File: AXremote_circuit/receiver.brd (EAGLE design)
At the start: 90 x 59 mm, 68 parts, among them IC1 MEGA8-AI, Q1 16MHz, Q2 12MHz, Q3 MOSFET-NCHANNELBSS138, U1 AX8052F143HS, X1 MINI-USB-SCHIELD-32005-201

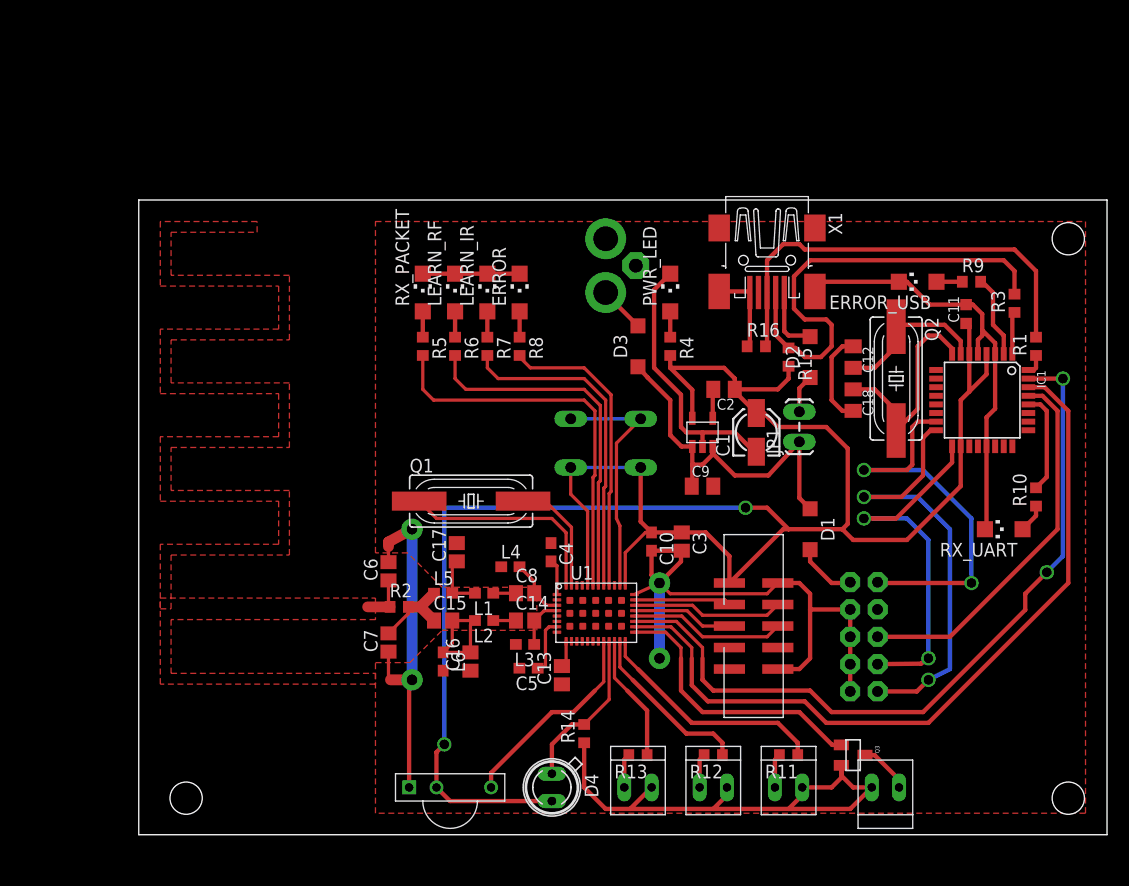
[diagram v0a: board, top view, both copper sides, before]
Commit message: Added a few keys.
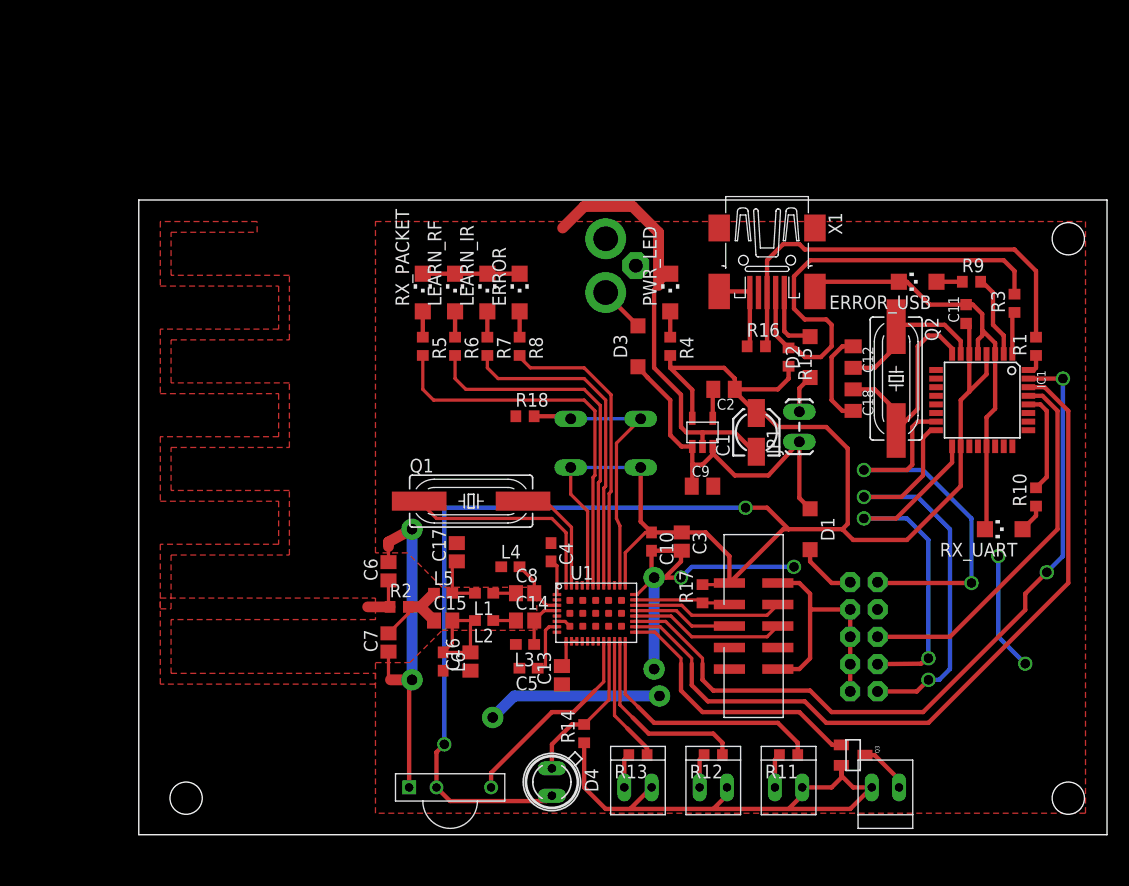
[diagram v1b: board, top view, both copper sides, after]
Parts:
- added R17, R18: 100, resistor:R0603
- moved D4 0.50 mm to (39.0, 5.50)
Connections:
- net GND: now also R18.1
- net N$27: now also R18.2
- net RST_N: now also R17.1
- net VCC: now also R17.2
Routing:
- net GND: track 234.6 -> 280.6 mm, vias 4 -> 10
- net N$27: track 23.0 -> 26.5 mm
- net VCC: track 199.0 -> 201.7 mm
- net N$40: track 16.0 -> 18.0 mm
- net N$39: track 21.9 -> 24.0 mm
- net N$47: track 25.9 -> 25.3 mm
- net UART_AXOUT: track 72.1 -> 71.5 mm
- net UART_AXIN: track 71.7 -> 71.1 mm
- net N$46: track 15.2 -> 14.7 mm
- net N$1: track 0.00 -> 0.50 mm

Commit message: Start work on receiver rev2.
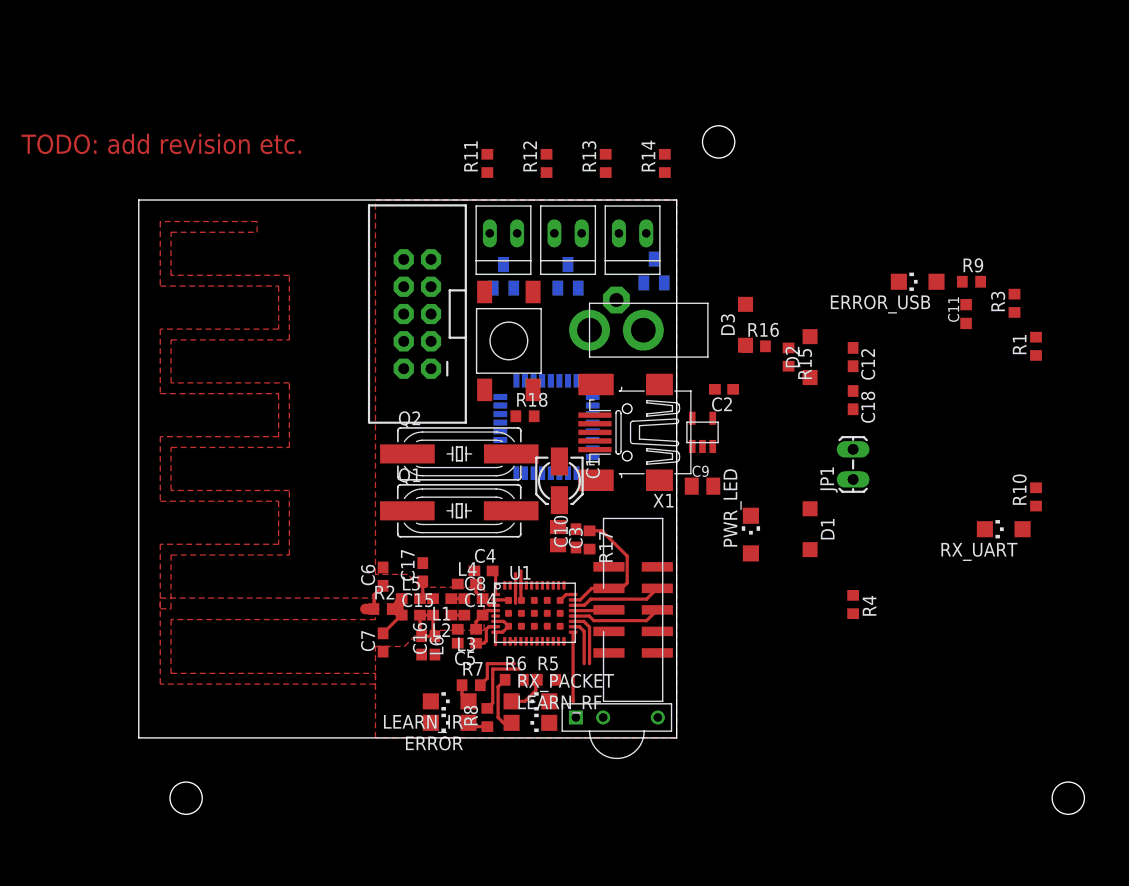
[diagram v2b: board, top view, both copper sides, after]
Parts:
- removed C13: 39pF, resistor:C0805
- removed D4: SFH482, led:SFH482
- removed S1: (no value), switch-omron:B3F-10XX
- added Q4, Q5: BC849SMD, transistor-npn:SOT23-BEC
- C12, C18, C2: device resistor:C0805K -> resistor:C0603
- C14, C15, C16, C17, C6, C7, C8: device resistor:C0805 -> resistor:C0603
- R12: value 100 -> ?
- R17: value 100 -> 10k
- U$7: value IR LED -> SWITCHSMD; device sam_eagle_parts:2PIN_PINHEADER -> sam:TACTILE_SWITCH_FSM2JSMA
- moved U$9 62.5 mm to (34.5, 56.5)
- moved R11 61.7 mm to (33.0, 63.0), turned to 90 degrees
- moved R12 57.1 mm to (38.5, 63.0), turned to 90 degrees
- moved Q3 55.1 mm to (34.5, 52.5), flipped to the bottom, turned to 0 degrees
- moved R13 55.1 mm to (44.0, 63.0), turned to 90 degrees
- moved R14 53.5 mm to (49.5, 63.0)
- moved U$5 53.5 mm to (46.5, 56.5), turned to 180 degrees
- moved U$6 53.2 mm to (40.5, 56.5), turned to 180 degrees
- moved U$2 51.2 mm to (26.5, 49.0), flipped to the top, turned to 180 degrees
- moved U$7 43.2 mm to (35.0, 46.5)
- moved Q2 41.2 mm to (30.4, 36.0), turned to 0 degrees
- moved LEARN_RF 40.6 mm to (37.0, 11.0), turned to 270 degrees
- moved IC1 40.6 mm to (38.5, 38.5), flipped to the bottom
- moved ERROR 40.5 mm to (29.5, 11.0), turned to 90 degrees
- moved RX_PACKET 39.3 mm to (37.0, 13.0), turned to 270 degrees
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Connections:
- removed net N$2: C13.2, U1.9
- removed net N$46: D4.A, R14.2, U1.17
- net GND: now also Q4.E, Q5.E, R14.2; no longer C13.1, R14.1, U$5.P$2, U$6.P$2, U$7.P$2
- net N$27: now also U$7.P3, U$7.P4; no longer S1.3, S1.4
- net N$39: now also Q4.C, U$5.P$2; no longer R11.1, U1.20
- net N$40: now also R13.1, U$6.P$1; no longer R12.1, U1.19
- net N$41: now also Q5.C, U$6.P$2; no longer R13.1, U1.18
- net N$42: now also R12.1, U1.20; no longer R13.2, U$7.P$1
- net N$43: now also Q4.B, Q5.B, R14.1; no longer U$6.P$1
- net VCC: now also R11.1, R13.2, U$7.P1, U$7.P2; no longer D4.K, S1.1, S1.2
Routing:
- net GND: track 280.6 -> 15.4 mm, vias 10 -> 0
- net VCC: track 201.7 -> 0.00 mm, vias 2 -> 0
- net UART_AXOUT: track 71.5 -> 4.21 mm
- net UART_AXIN: track 71.1 -> 5.15 mm, vias 2 -> 0
- net D-: track 43.2 -> 0.00 mm
- net N$21: track 41.2 -> 0.00 mm, vias 2 -> 0
- net D+: track 40.9 -> 0.00 mm
- net N$23: track 37.2 -> 0.00 mm, vias 2 -> 0
- net N$26: track 36.3 -> 0.00 mm
- net N$19: track 35.2 -> 0.00 mm
- net N$22: track 34.6 -> 0.00 mm, vias 2 -> 0
- net VCC_IN: track 34.4 -> 0.00 mm
- net N$31: track 33.5 -> 0.00 mm
- net N$27: track 26.5 -> 0.00 mm
- net N$32: track 30.7 -> 4.77 mm
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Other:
- board size 90 x 59 mm -> 50 x 50 mm
- board text added: "TODO: add revision etc."

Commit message: Replace AVR with FT121 on receiver. Other details.
- Clean up schematics
- Use every pin of F143 (second button, GPIO)
- add TXCO and XTAL
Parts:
- removed D1, D2, D3: (no value), diode:SOD123
- removed ERROR_USB: rot, led:CHIPLED_1206
- removed IC1: MEGA8-AI, atmel:TQFP32-08
- removed Q2: 12MHz, crystal:SM49
- removed Q4: BC849SMD, transistor-npn:SOT23-BEC
- removed RX_UART: grün, led:CHIPLED_1206
- added BEAD: ferrite, resistor:R0603
- added C13: 47pF, resistor:C0603K
- added C19: 100nF, resistor:C0603K
- added C20, C21: 100n, resistor:C0603
- added R19: 10k, resistor:R0603
- added U$10: SWITCHSMD, sam:TACTILE_SWITCH_FSM2JSMA
- added X2: (no value), axsem_osc_v1-2:X3225
- C12: value 27pF -> 47pF; device resistor:C0603 -> resistor:C0603K
- C18: value 27pF -> 10nF; device resistor:C0603 -> resistor:C0603K
- JP1: value M02LOCK_LONGPADS -> (none); device SparkFun-Connectors:1X02_LOCK_LONGPADS -> jumper:JP2
- R1, R3: value 68 -> 27
- R10: value 68 -> 10k
- R15: value 1k5 -> 100
- R16: value 1M -> NC
- R9: value 100 -> 10k
- U$2: value AVR_SPI_PROG2PTH2 -> FT121; device SparkFun-Connectors:2X5-SHROUDED -> sam:TSSOP16
- moved R10 59.5 mm to (26.2, 46.2), turned to 0 degrees
- moved R15 57.6 mm to (25.0, 0.00), turned to 0 degrees
- moved R9 51.8 mm to (26.2, 51.4)
- moved C12 47.2 mm to (26.2, 68.8), turned to 0 degrees
- moved C18 45.2 mm to (26.2, 60.4), turned to 0 degrees
- moved JP1 42.7 mm to (34.5, 6.00), turned to 180 degrees
- moved R16 29.3 mm to (31.5, 33.5)
- moved U$1 18.9 mm to (38.0, 49.5)
- moved U$2 15.2 mm to (36.5, 37.5), turned to 90 degrees
- moved C1 13.4 mm to (27.0, 37.7), turned to 0 degrees
- moved R18 9.55 mm to (27.0, 40.5)
- moved U$7 2.06 mm to (33.0, 47.0)
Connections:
- removed net N$23: IC1.15, U$2.1
- removed net N$24: D1.A, U$2.2
- removed net N$34: ERROR_USB.A, R9.1
- removed net N$35: IC1.2, R9.2
- removed net N$36: R10.1, RX_UART.A
- removed net N$38: D3.A, U$4.P1:PIN
- removed net N$39: Q4.C, U$5.P$2
- removed net N$45: U$8.P3:OUT, U1.16
- removed net N$49: D2.C, JP1.2
- removed net N$50: IC1.28, R10.2
- removed net UART_AXIN: IC1.31, U1.23
- removed net UART_AXOUT: IC1.30, U1.22
- new net FTDI_!RESET: R9.2, U$2.11, U1.18
- new net FTDI_SUSPEND: R10.2, U$2.6, U1.19
- new net N$2: R1.1, U$2.16
- new net SPI_!INT: U$2.7, U1.13
- new net SPI_!SS: U$2.3, U1.17
- new net SPI_MISO: U$2.8, U1.14
- new net SPI_MOSI: U$2.9, U1.15
- new net SPI_SCLK: U$2.2, U1.16
- net D+: now also C13.1; no longer R16.2
- net D-: now also C12.1; no longer R15.1
- net GND: now also C12.2, C13.2, C18.1, C19.1, C20.2, JP1.3, R15.1, U$2.14, X2.2; no longer C12.1, C18.2, ERROR_USB.C, IC1.21, IC1.3, IC1.5, Q4.E, RX_UART.C, U$2.10, U$2.6, U$2.8
- net N$11: now also BEAD.1, C11.1, U$2.13; no longer C18.1, IC1.8, Q2.2
- net N$14: now also R19.2
- net N$15: now also C21.1, R19.1
- net N$16: now also JP1.1, U1.22; no longer IC1.32, R1.1
- net N$17: now also R15.2, U$10.P3, U$10.P4, U1.31; no longer IC1.1, R3.1
- net N$19: now also R16.2, X2.1; no longer IC1.29, U$2.5
- net N$21: now also U$8.P3:OUT, U1.21; no longer IC1.16, U$2.9
- net N$22: now also C21.2, X2.3; no longer IC1.17, U$2.7
- net N$41: now also U$5.P$2
- net N$43: no longer Q4.B
- net N$47: now also U1.23; no longer U1.21
- net N$5: now also R3.1, U$2.15; no longer C12.2, IC1.7, Q2.1
- net VCC: now also C19.2, C20.1, JP1.2, R10.1, R9.1, U$10.P1, U$10.P2, U$2.10, U$2.12, U$2.5, X2.4; no longer C11.1, IC1.18, IC1.4, IC1.6, R15.2
- net VCC_IN: now also U$4.P1:PIN; no longer D1.C, D3.C, JP1.1
- net VCC_USB: now also BEAD.2, C18.2; no longer D2.A
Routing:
- net N$47: track 6.44 -> 0.00 mm
- net UART_AXIN: track 5.15 -> 0.00 mm
- net UART_AXOUT: track 4.21 -> 0.00 mm
- net RST_N: track 12.7 -> 10.8 mm
- net DBG_DATA: track 8.42 -> 7.01 mm

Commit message: Started routing receiver rev2.
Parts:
- U$2: value FT121 -> FT121FTDI; device sam:TSSOP16 -> sam:TSSOP16-FTDI
- moved R15 48.1 mm to (32.5, 47.5), turned to 90 degrees
- moved R1 44.8 mm to (39.8, 38.4), turned to 0 degrees
- moved R3 44.2 mm to (39.8, 37.0), turned to 0 degrees
- moved C11 42.5 mm to (37.2, 35.4), turned to 270 degrees
- moved ERROR 41.3 mm to (64.5, 33.0), turned to 180 degrees
- moved LEARN_RF 40.3 mm to (64.5, 40.5), turned to 0 degrees
- moved BEAD 40.2 mm to (39.8, 35.6)
- moved R8 39.8 mm to (64.0, 36.5), turned to 180 degrees
- moved R9 39.2 mm to (38.0, 14.0)
- moved LEARN_IR 38.6 mm to (62.5, 33.0), turned to 180 degrees
- moved RX_PACKET 37.5 mm to (62.5, 40.5), turned to 0 degrees
- moved R7 35.9 mm to (61.0, 35.0), turned to 90 degrees
- moved R10 35.4 mm to (41.0, 14.0), turned to 180 degrees
- moved R5 34.8 mm to (60.5, 42.0), turned to 90 degrees
- moved R6 34.7 mm to (60.5, 39.0), turned to 90 degrees
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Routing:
- net VCC: track 0.00 -> 76.7 mm, vias 0 -> 3
- net SPI_SCLK: track 0.00 -> 44.1 mm, vias 0 -> 2
- net SPI_!SS: track 0.00 -> 41.8 mm, vias 0 -> 2
- net FTDI_SUSPEND: track 0.00 -> 40.5 mm, vias 0 -> 2
- net SPI_!INT: track 0.00 -> 40.0 mm, vias 0 -> 2
- net SPI_MOSI: track 0.00 -> 38.7 mm, vias 0 -> 2
- net FTDI_!RESET: track 0.00 -> 37.8 mm, vias 0 -> 2
- net SPI_MISO: track 0.00 -> 36.7 mm, vias 0 -> 2
- net N$42: track 0.00 -> 21.3 mm, vias 0 -> 1
- net N$15: track 0.00 -> 16.1 mm
- net N$16: track 0.00 -> 15.0 mm
- net D-: track 0.00 -> 11.1 mm
- net N$21: track 0.00 -> 9.73 mm
- net GND: track 15.4 -> 24.3 mm, vias 0 -> 36
- net N$47: track 0.00 -> 7.21 mm
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
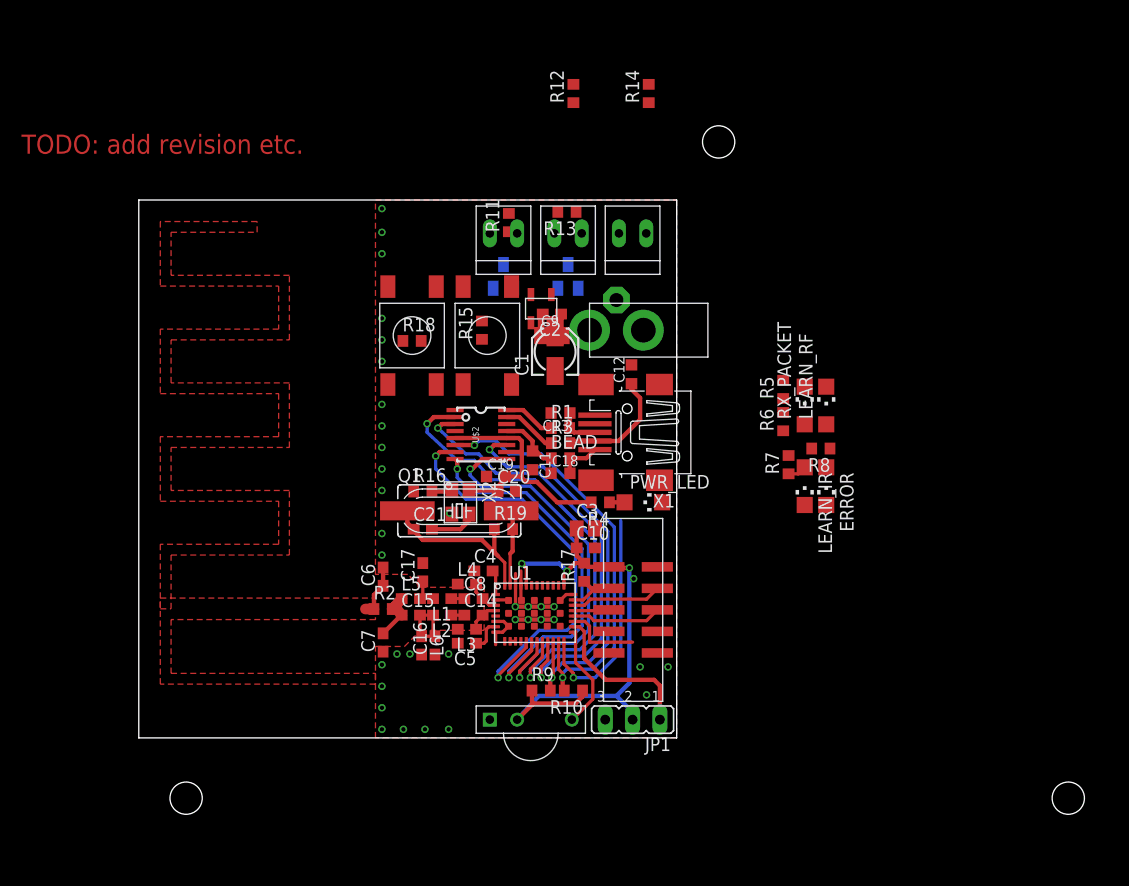
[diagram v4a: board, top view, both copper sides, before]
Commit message: Routed receiver rev2.
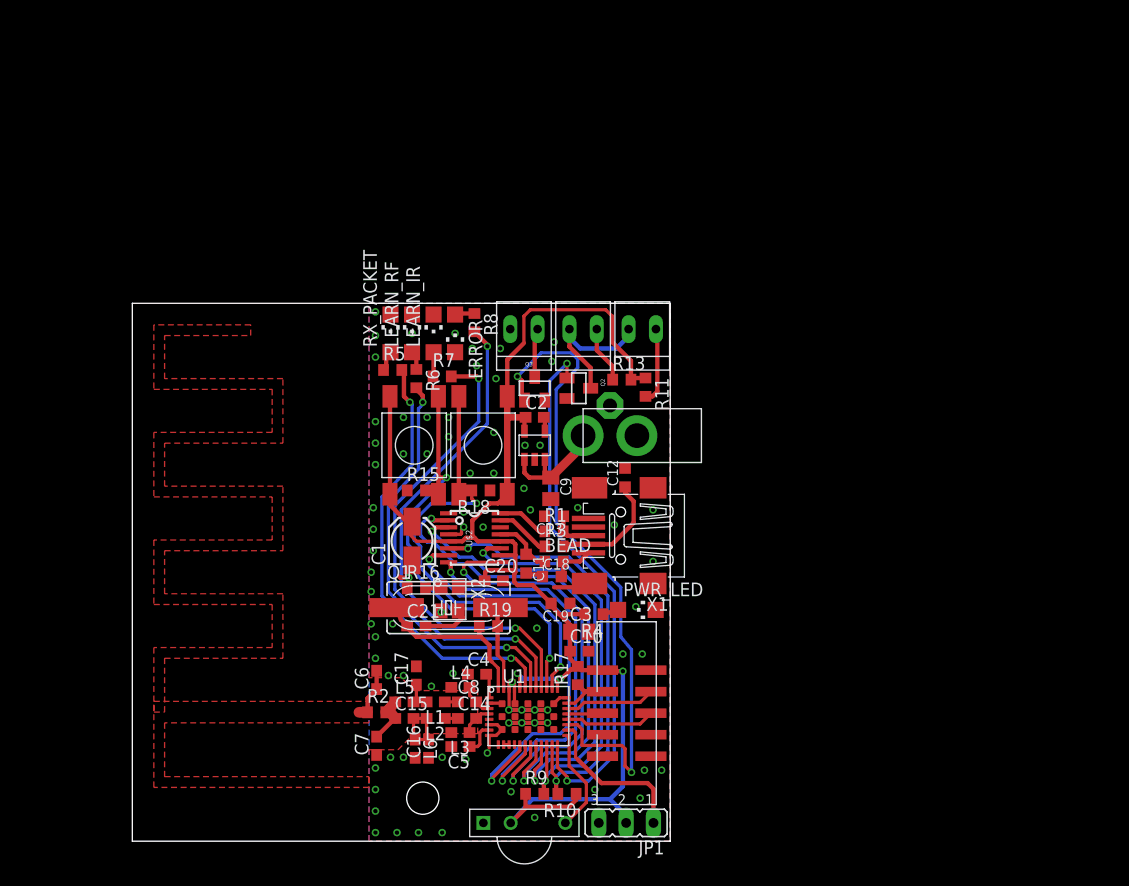
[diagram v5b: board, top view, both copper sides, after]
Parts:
- removed Q5: BC849SMD, transistor-npn:SOT23-BEC
- removed R12: ?, resistor:R0603
- removed R14: 10k, resistor:R0603
- added Q2: MOSFET-NCHANNELBSS138, SparkFun-DiscreteSemi:SOT23
- moved LEARN_RF 39.1 mm to (26.0, 47.2)
- moved RX_PACKET 39.1 mm to (24.0, 47.2)
- moved ERROR 37.3 mm to (30.0, 47.2)
- moved LEARN_IR 37.3 mm to (28.0, 47.2), turned to 0 degrees
- moved R5 36.3 mm to (24.2, 43.8), turned to 0 degrees
- moved R6 34.3 mm to (26.4, 43.0), turned to 270 degrees
- moved R8 34.3 mm to (31.8, 48.2), turned to 270 degrees
- moved R7 33.2 mm to (28.8, 43.2), turned to 0 degrees
- moved C1 22.1 mm to (26.0, 27.9)
- moved R11 19.9 mm to (47.7, 42.2), turned to 270 degrees
- moved R13 16.4 mm to (45.5, 42.9), turned to 0 degrees
- moved R15 16.1 mm to (26.4, 32.6), turned to 0 degrees
- moved R18 15.3 mm to (32.4, 32.6), turned to 180 degrees
- moved C9 14.2 mm to (38.9, 32.8), turned to 270 degrees
- moved C19 13.2 mm to (39.8, 22.1), turned to 180 degrees
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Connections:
- removed net N$43: Q5.B, R12.2, R14.1
- net GND: now also Q2.2; no longer Q5.E, R14.2
- net N$41: now also Q2.3; no longer Q5.C
- net N$42: now also Q2.1; no longer R12.1
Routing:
- net VCC: track 76.7 -> 141.1 mm
- net N$47: track 7.21 -> 61.0 mm, vias 0 -> 2
- net N$33: track 0.00 -> 46.5 mm, vias 0 -> 2
- net N$27: track 0.00 -> 44.4 mm, vias 0 -> 2
- net N$32: track 0.00 -> 44.1 mm, vias 0 -> 2
- net N$17: track 0.00 -> 42.7 mm, vias 0 -> 2
- net N$26: track 0.00 -> 40.6 mm, vias 0 -> 2
- net N$31: track 0.00 -> 38.9 mm, vias 0 -> 2
- net N$42: track 21.3 -> 50.0 mm, vias 1 -> 2
- net N$41: track 0.00 -> 14.2 mm
- net VCC_IN: track 0.00 -> 11.2 mm
- net N$37: track 0.00 -> 7.14 mm
- net GND: track 24.3 -> 31.3 mm, vias 36 -> 80
- net N$40: track 0.00 -> 5.31 mm
- net N$48: track 0.00 -> 4.51 mm
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- added copper zone on layer 16, net GND
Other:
- board text added: "AXreceiver"
- board text added: "Samuel Bryner (2014, rev 2)"
- board text removed: "TODO: add revision etc."
